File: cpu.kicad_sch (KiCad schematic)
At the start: 33 parts, among them IC12 DS2401+, IC13 ARM250, IC20 74HC138, IC27 74AC32, IC8 74HCT14, X4 72.0MHz, X5 25.175MHz

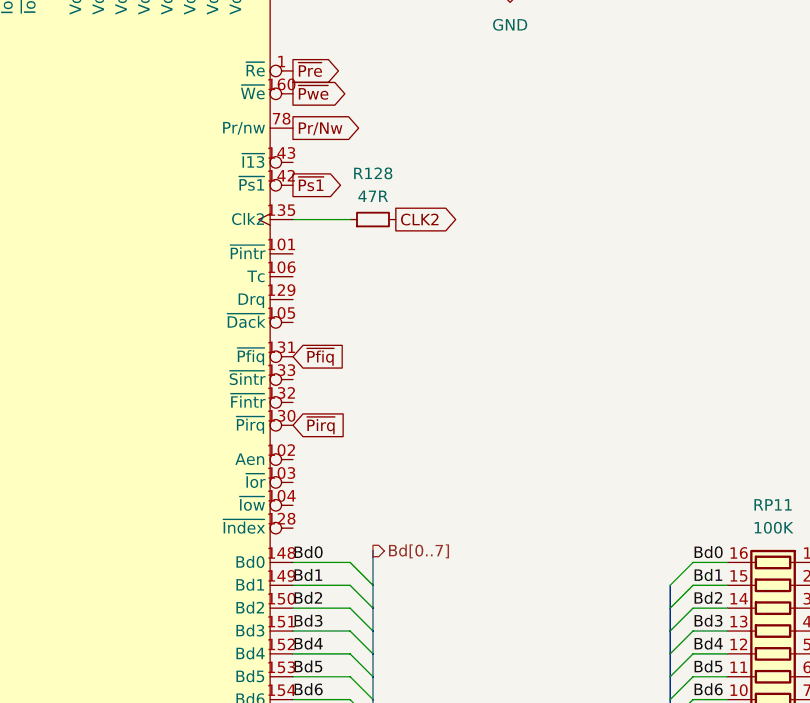
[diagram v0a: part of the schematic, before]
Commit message: add io details
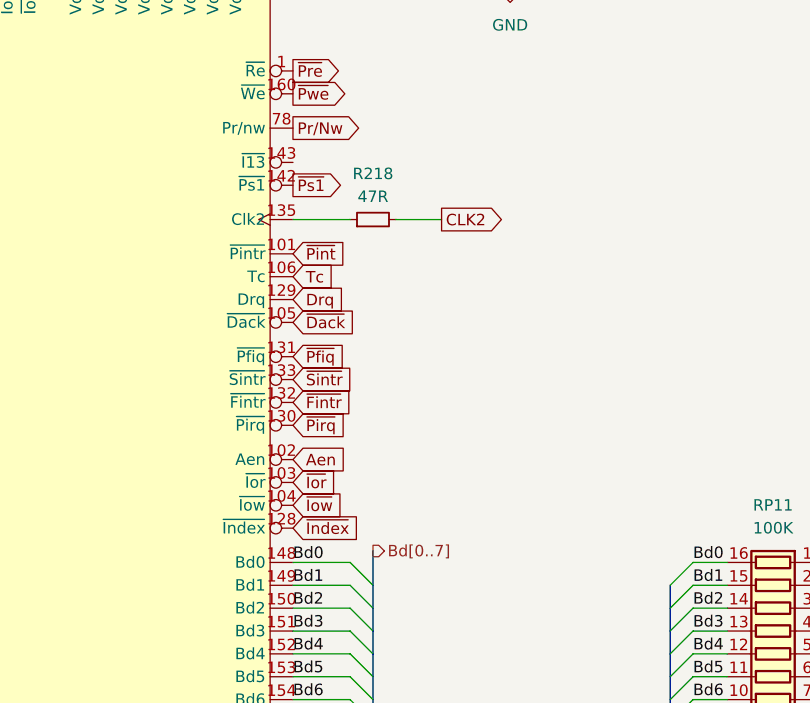
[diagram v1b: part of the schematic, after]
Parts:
- renumbered R128 to R218
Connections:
- net ~{Pint}: now reaches IC13.101 (~{Pintr})
- net Aen: now reaches IC13.102 (Aen)
- net ~{Ior}: now reaches IC13.103 (~{Ior})
- net ~{Iow}: now reaches IC13.104 (~{Iow})
- net ~{Dack}: now reaches IC13.105 (~{Dack})
- net Tc: now reaches IC13.106 (Tc)
- net ~{Index}: now reaches IC13.128 (~{Index})
- net Drq: now reaches IC13.129 (Drq)
- net ~{Fintr}: now reaches IC13.132 (~{Fintr})
- net ~{Sintr}: now reaches IC13.133 (~{Sintr})
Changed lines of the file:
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@@
 	(wire
 		(pts
+			(xy 226.06 115.57) (xy 220.98 115.57)
+		)
+		(stroke
+			(width 0)
+			(type default)
+		)
+	)
+	(wire
+		(pts
 			(xy 254 166.37) (xy 257.81 166.37)
 		)
@@
 		)
 	)
+	(global_label "~{Pint}"
+		(shape input)
+		(at 209.55 119.38 0)
+		(fields_autoplaced yes)
+		(effects
+			(font
+				(size 1.27 1.27)
+			)
+			(justify left)
+		)
+		(property "Intersheetrefs" "${INTERSHEET_REFS}"
+			(at 216.2847 119.38 0)
+			(effects
+				(font
+					(size 1.27 1.27)
+				)
+				(justify left)
+				(hide yes)
+			)
+		)
+	)
+	(global_label "~{Fintr}"
+		(shape input)
+		(at 209.55 135.89 0)
+		(fields_autoplaced yes)
+		(effects
+			(font
+				(size 1.27 1.27)
+			)
+			(justify left)
+		)
+		(property "Intersheetrefs" "${INTERSHEET_REFS}"
+			(at 216.8895 135.89 0)
+			(effects
+				(font
+					(size 1.27 1.27)
+				)
+				(justify left)
+				(hide yes)
+			)
+		)
+	)
 	(global_label "~{Joyst2}"
 		(shape output)
@@
 		)
 	)
+	(global_label "~{Index}"
+		(shape input)
+		(at 209.55 149.86 0)
+		(fields_autoplaced yes)
+		(effects
+			(font
+				(size 1.27 1.27)
+			)
+			(justify left)
+		)
+		(property "Intersheetrefs" "${INTERSHEET_REFS}"
+			(at 217.5547 149.86 0)
+			(effects
+				(font
+					(size 1.27 1.27)
+				)
+				(justify left)
+				(hide yes)
+			)
+		)
+	)
 	(global_label "~{Pfiq}"
 		(shape input)
@@
 		)
 	)
+	(global_label "~{Sintr}"
+		(shape input)
+		(at 209.55 133.35 0)
+		(fields_autoplaced yes)
+		(effects
+			(font
+				(size 1.27 1.27)
+			)
+			(justify left)
+		)
+		(property "Intersheetrefs" "${INTERSHEET_REFS}"
+			(at 217.0104 133.35 0)
+			(effects
+				(font
+					(size 1.27 1.27)
+				)
+				(justify left)
+				(hide yes)
+			)
+		)
+	)
+	(global_label "~{Dack}"
+		(shape input)
+		(at 209.55 127 0)
+		(fields_autoplaced yes)
+		(effects
+			(font
+				(size 1.27 1.27)
+			)
+			(justify left)
+		)
+		(property "Intersheetrefs" "${INTERSHEET_REFS}"
+			(at 217.0709 127 0)
+			(effects
+				(font
+					(size 1.27 1.27)
+				)
+				(justify left)
+				(hide yes)
+			)
+		)
+	)
+	(global_label "Aen"
+		(shape input)
+		(at 209.55 142.24 0)
+		(fields_autoplaced yes)
+		(effects
+			(font
+				(size 1.27 1.27)
+			)
+			(justify left)
+		)
+		(property "Intersheetrefs" "${INTERSHEET_REFS}"
+			(at 215.8614 142.24 0)
+			(effects
+				(font
+					(size 1.27 1.27)
+				)
+				(justify left)
+				(hide yes)
+			)
+		)
+	)
 	(global_label "CLK2"
 		(shape output)
-		(at 220.98 115.57 0)
+		(at 226.06 115.57 0)
 		(fields_autoplaced yes)
 		(effects
@@
 		)
 		(property "Intersheetrefs" "${INTERSHEET_REFS}"
-			(at 228.7428 115.57 0)
+			(at 233.8228 115.57 0)
 			(effects
 				(font
@@
 		)
 	)
+	(global_label "Tc"
+		(shape input)
+		(at 209.55 121.92 0)
+		(fields_autoplaced yes)
+		(effects
+			(font
+				(size 1.27 1.27)
+			)
+			(justify left)
+		)
+		(property "Intersheetrefs" "${INTERSHEET_REFS}"
+			(at 214.5914 121.92 0)
+			(effects
+				(font
+					(size 1.27 1.27)
+				)
+				(justify left)
+				(hide yes)
+			)
+		)
+	)
 	(global_label "~{Mcras}"
 		(shape output)
@@
 		)
 	)
+	(global_label "~{Iow}"
+		(shape input)
+		(at 209.55 147.32 0)
+		(fields_autoplaced yes)
+		(effects
+			(font
+				(size 1.27 1.27)
+			)
+			(justify left)
+		)
+		(property "Intersheetrefs" "${INTERSHEET_REFS}"
+			(at 215.6195 147.32 0)
+			(effects
+				(font
+					(size 1.27 1.27)
+				)
+				(justify left)
+				(hide yes)
+			)
+		)
+	)
+	(global_label "Drq"
+		(shape input)
+		(at 209.55 124.46 0)
+		(fields_autoplaced yes)
+		(effects
+			(font
+				(size 1.27 1.27)
+			)
+			(justify left)
+		)
+		(property "Intersheetrefs" "${INTERSHEET_REFS}"
+			(at 215.7404 124.46 0)
+			(effects
+				(font
+					(size 1.27 1.27)
+				)
+				(justify left)
+				(hide yes)
+			)
+		)
+	)
 	(global_label "~{Romcs}"
 		(shape input)
@@
 		)
 	)
+	(global_label "~{Ior}"
+		(shape input)
+		(at 209.55 144.78 0)
+		(fields_autoplaced yes)
+		(effects
+			(font
+				(size 1.27 1.27)
+			)
+			(justify left)
+		)
+		(property "Intersheetrefs" "${INTERSHEET_REFS}"
+			(at 215.0752 144.78 0)
+			(effects
+				(font
+					(size 1.27 1.27)
+				)
+				(justify left)
+				(hide yes)
+			)
+		)
+	)
 	(global_label "HS"
 		(shape output)
@@
 		(dnp no)
 		(fields_autoplaced yes)
-		(property "Reference" "R128"
+		(property "Reference" "R218"
 			(at 218.44 110.49 90)
 			(effects
@@
 			(project "Acorn-A3010"
 				(path "/999882f3-94f8-4a89-9093-27a47d0cb289/5f74aac3-9761-4bed-8486-119acb837e61"
-					(reference "R128")
+					(reference "R218")
 					(unit 1)
 				)

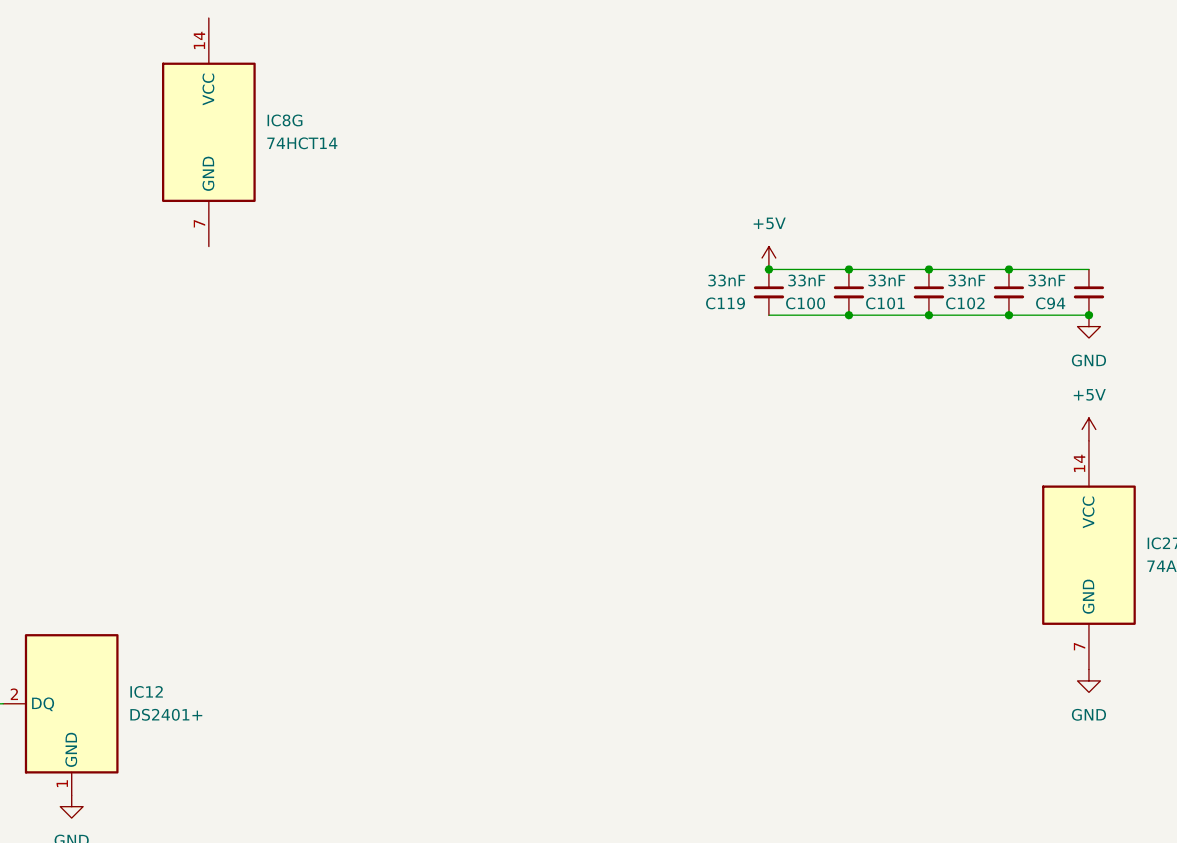
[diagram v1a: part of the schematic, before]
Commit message: data path routing
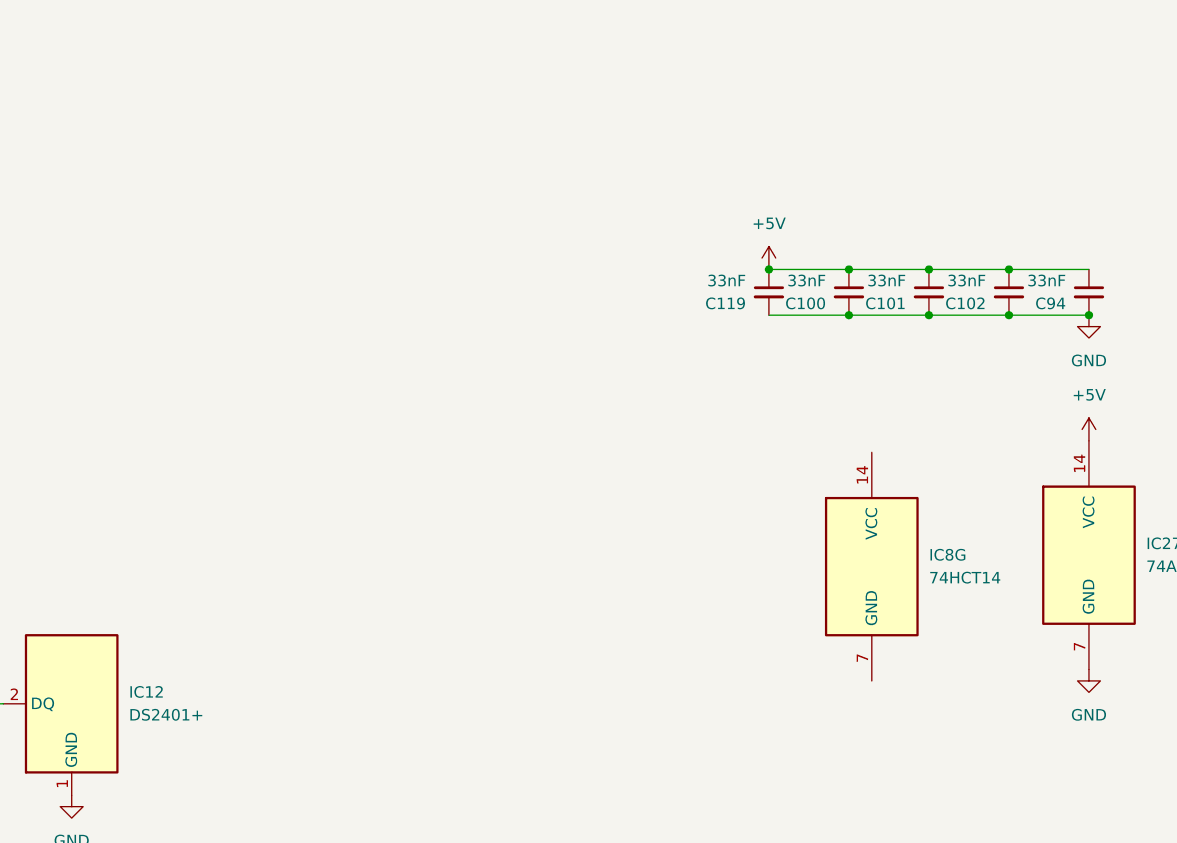
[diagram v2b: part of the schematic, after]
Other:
- moved on the sheet: IC8G
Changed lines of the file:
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@@
 	(symbol
 		(lib_id "74xx:74LS14")
-		(at 248.92 15.24 0)
+		(at 322.58 63.5 0)
 		(unit 7)
 		(exclude_from_sim no)
@@
 		(fields_autoplaced yes)
 		(property "Reference" "IC8"
-			(at 255.27 13.9699 0)
+			(at 328.93 62.2299 0)
 			(effects
 				(font
@@
 		)
 		(property "Value" "74HCT14"
-			(at 255.27 16.5099 0)
+			(at 328.93 64.7699 0)
 			(effects
 				(font
@@
 		)
 		(property "Footprint" "Package_SO:SOIC-14_3.9x8.7mm_P1.27mm"
-			(at 248.92 15.24 0)
+			(at 322.58 63.5 0)
 			(effects
 				(font
@@
 		)
 		(property "Datasheet" "http://www.ti.com/lit/gpn/sn74LS14"
-			(at 248.92 15.24 0)
+			(at 322.58 63.5 0)
 			(effects
 				(font
@@
 		)
 		(property "Description" "Hex inverter schmitt trigger"
-			(at 248.92 15.24 0)
+			(at 322.58 63.5 0)
 			(effects
 				(font

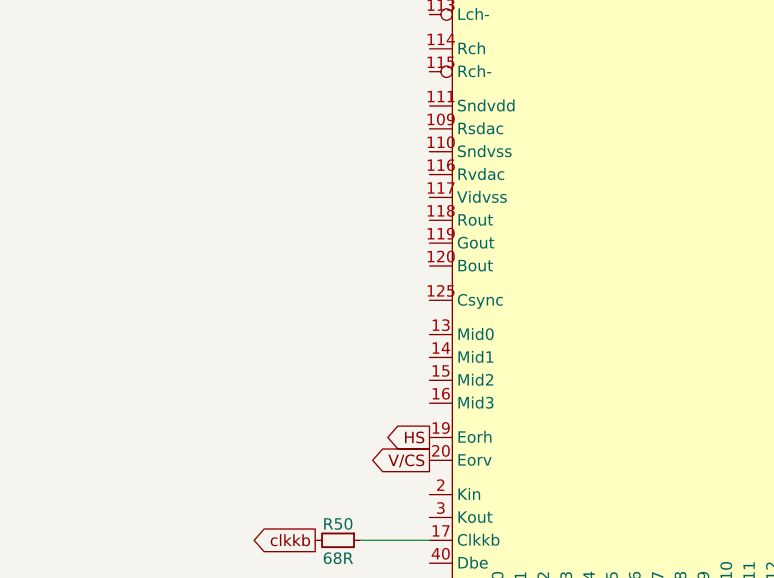
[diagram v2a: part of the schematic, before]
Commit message: add digital video schematic
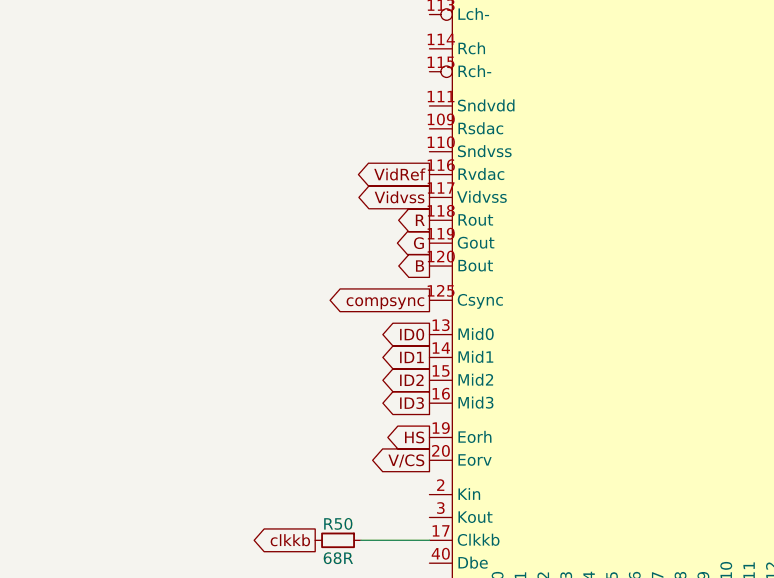
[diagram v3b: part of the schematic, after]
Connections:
- net VidRef: now reaches IC13.116 (Rvdac)
- net Vidvss: now reaches IC13.117 (Vidvss)
- net R: now reaches IC13.118 (Rout)
- net G: now reaches IC13.119 (Gout)
- net B: now reaches IC13.120 (Bout)
- net compsync: now reaches IC13.125 (Csync)
- net ID0: now reaches IC13.13 (Mid0)
- net ID1: now reaches IC13.14 (Mid1)
- net ID2: now reaches IC13.15 (Mid2)
- net ID3: now reaches IC13.16 (Mid3)
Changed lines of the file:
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@@
+		)
+	)
+	(global_label "B"
+		(shape output)
+		(at 92.71 193.04 180)
+		(fields_autoplaced yes)
+		(effects
+			(font
+				(size 1.27 1.27)
+			)
+			(justify right)
+		)
+		(property "Intersheetrefs" "${INTERSHEET_REFS}"
+			(at 88.4548 193.04 0)
+			(effects
+				(font
+					(size 1.27 1.27)
+				)
+				(justify right)
+				(hide yes)
+			)
 		)
 	)
@@
 		)
 	)
+	(global_label "compsync"
+		(shape output)
+		(at 92.71 196.85 180)
+		(fields_autoplaced yes)
+		(effects
+			(font
+				(size 1.27 1.27)
+			)
+			(justify right)
+		)
+		(property "Intersheetrefs" "${INTERSHEET_REFS}"
+			(at 80.4116 196.85 0)
+			(effects
+				(font
+					(size 1.27 1.27)
+				)
+				(justify right)
+				(hide yes)
+			)
+		)
+	)
 	(global_label "C0"
 		(shape input)
@@
 		)
 	)
+	(global_label "Vidvss"
+		(shape output)
+		(at 92.71 185.42 180)
+		(fields_autoplaced yes)
+		(effects
+			(font
+				(size 1.27 1.27)
+			)
+			(justify right)
+		)
+		(property "Intersheetrefs" "${INTERSHEET_REFS}"
+			(at 83.8586 185.42 0)
+			(effects
+				(font
+					(size 1.27 1.27)
+				)
+				(justify right)
+				(hide yes)
+			)
+		)
+	)
+	(global_label "ID2"
+		(shape output)
+		(at 92.71 205.74 180)
+		(fields_autoplaced yes)
+		(effects
+			(font
+				(size 1.27 1.27)
+			)
+			(justify right)
+		)
+		(property "Intersheetrefs" "${INTERSHEET_REFS}"
+			(at 86.6405 205.74 0)
+			(effects
+				(font
+					(size 1.27 1.27)
+				)
+				(justify right)
+				(hide yes)
+			)
+		)
+	)
 	(global_label "~{Dack}"
 		(shape input)
@@
 		)
 	)
+	(global_label "ID3"
+		(shape output)
+		(at 92.71 208.28 180)
+		(fields_autoplaced yes)
+		(effects
+			(font
+				(size 1.27 1.27)
+			)
+			(justify right)
+		)
+		(property "Intersheetrefs" "${INTERSHEET_REFS}"
+			(at 86.6405 208.28 0)
+			(effects
+				(font
+					(size 1.27 1.27)
+				)
+				(justify right)
+				(hide yes)
+			)
+		)
+	)
+	(global_label "G"
+		(shape output)
+		(at 92.71 190.5 180)
+		(fields_autoplaced yes)
+		(effects
+			(font
+				(size 1.27 1.27)
+			)
+			(justify right)
+		)
+		(property "Intersheetrefs" "${INTERSHEET_REFS}"
+			(at 88.4548 190.5 0)
+			(effects
+				(font
+					(size 1.27 1.27)
+				)
+				(justify right)
+				(hide yes)
+			)
+		)
+	)
 	(global_label "~{Ras1}"
 		(shape output)
@@
 		)
 	)
+	(global_label "ID1"
+		(shape output)
+		(at 92.71 203.2 180)
+		(fields_autoplaced yes)
+		(effects
+			(font
+				(size 1.27 1.27)
+			)
+			(justify right)
+		)
+		(property "Intersheetrefs" "${INTERSHEET_REFS}"
+			(at 86.6405 203.2 0)
+			(effects
+				(font
+					(size 1.27 1.27)
+				)
+				(justify right)
+				(hide yes)
+			)
+		)
+	)
 	(global_label "~{Pirq}"
 		(shape input)
@@
 		)
 	)
+	(global_label "ID0"
+		(shape output)
+		(at 92.71 200.66 180)
+		(fields_autoplaced yes)
+		(effects
+			(font
+				(size 1.27 1.27)
+			)
+			(justify right)
+		)
+		(property "Intersheetrefs" "${INTERSHEET_REFS}"
+			(at 86.6405 200.66 0)
+			(effects
+				(font
+					(size 1.27 1.27)
+				)
+				(justify right)
+				(hide yes)
+			)
+		)
+	)
 	(global_label "~{Iogt}"
 		(shape output)
@@
 				(hide yes)
 			)
+		)
+	)
+	(global_label "VidRef"
+		(shape output)
+		(at 92.71 182.88 180)
+		(fields_autoplaced yes)
+		(effects
+			(font
+				(size 1.27 1.27)
+			)
+			(justify right)
+		)
+		(property "Intersheetrefs" "${INTERSHEET_REFS}"
+			(at 83.7981 182.88 0)
+			(effects
+				(font
+					(size 1.27 1.27)
+				)
+				(justify right)
+				(hide yes)
+			)
+		)
+	)
+	(global_label "R"
+		(shape output)
+		(at 92.71 187.96 180)
+		(fields_autoplaced yes)
+		(effects
+			(font
+				(size 1.27 1.27)
+			)
+			(justify right)
+		)
+		(property "Intersheetrefs" "${INTERSHEET_REFS}"
+			(at 88.4548 187.96 0)
+			(effects
+				(font
+					(size 1.27 1.27)
+				)
+				(justify right)
+				(hide yes)
+			)
